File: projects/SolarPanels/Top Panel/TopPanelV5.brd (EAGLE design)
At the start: 99.5 x 99.5 mm, 41 parts

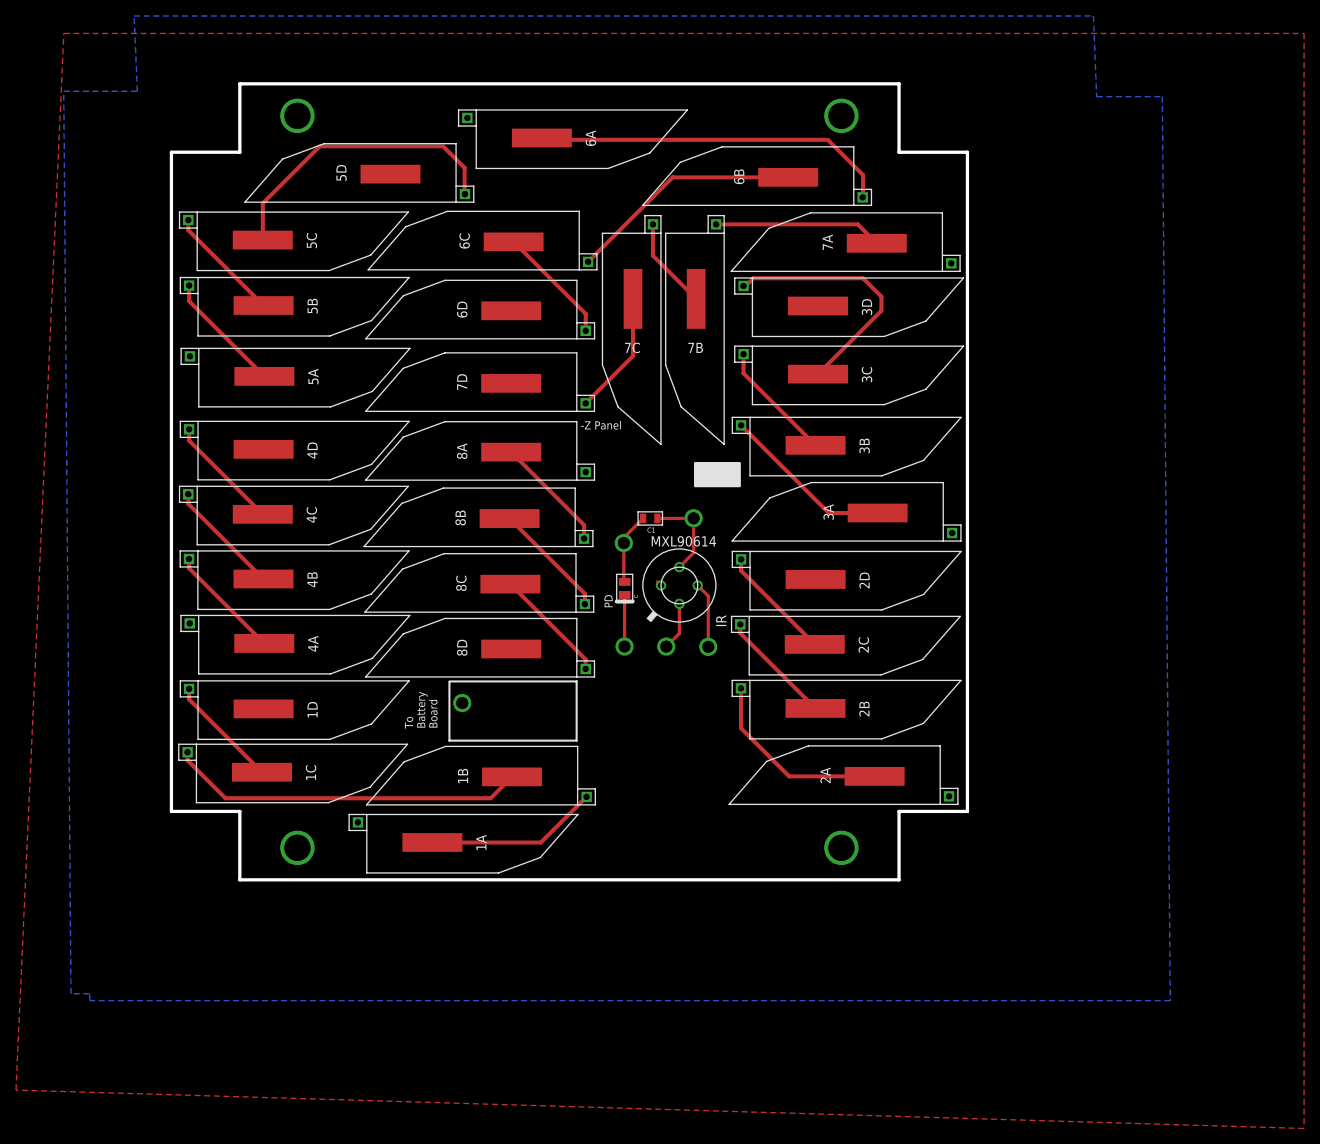
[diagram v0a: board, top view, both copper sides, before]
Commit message: Completed TopPanelV5 with new board dimensions and cells. Ready for rewview/fab
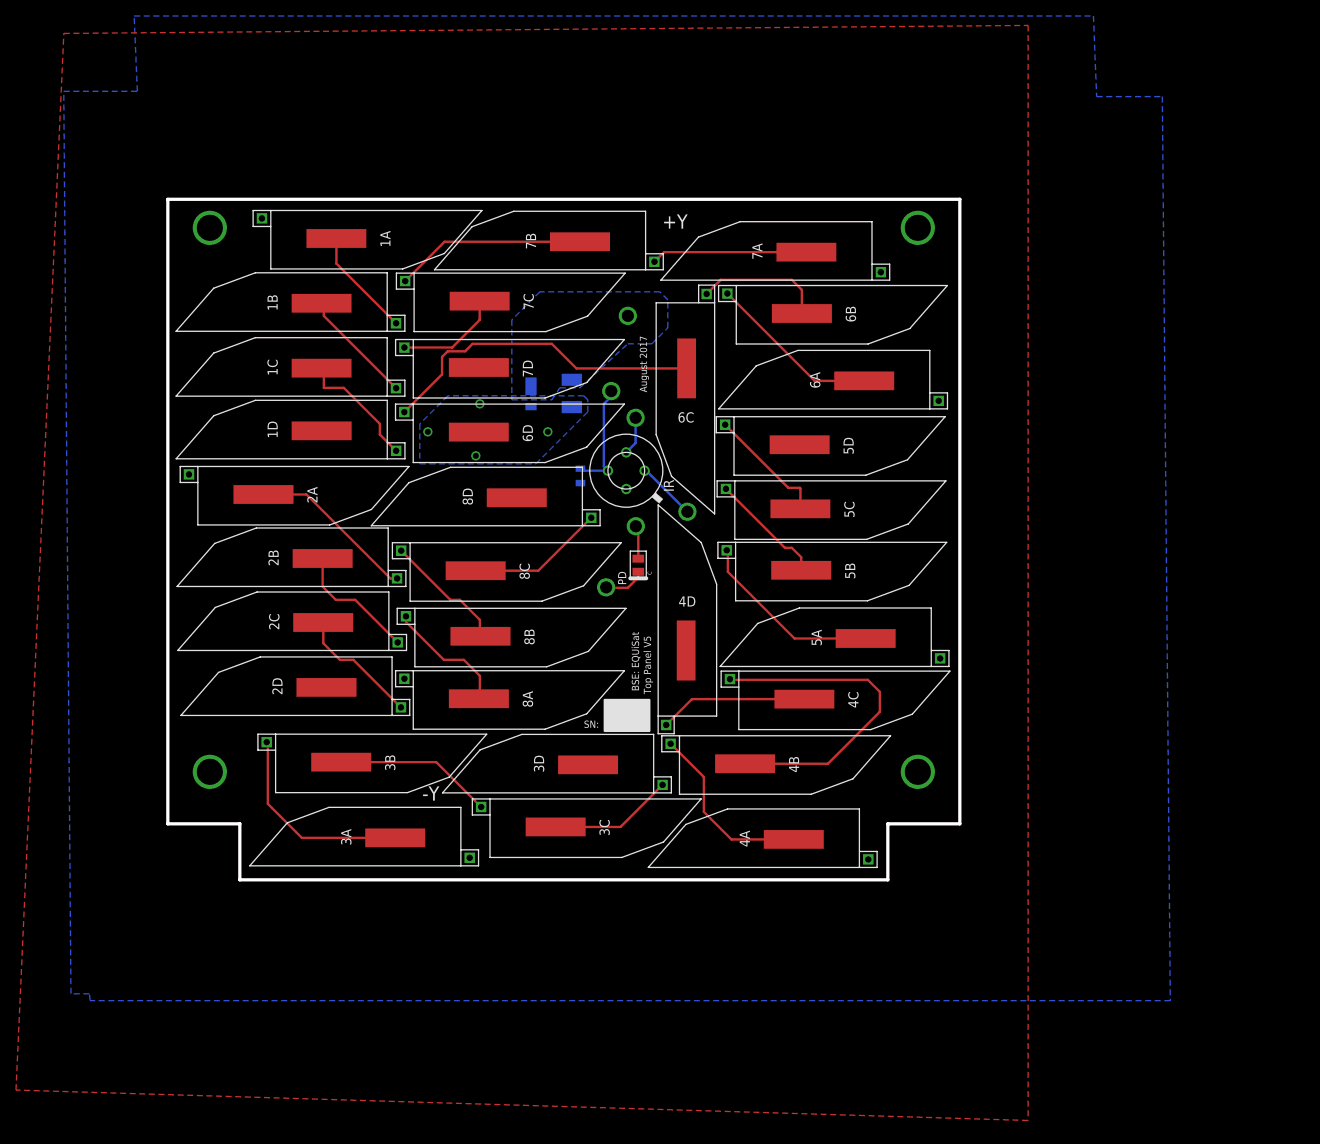
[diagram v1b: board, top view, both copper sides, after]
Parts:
- added D1: DFLS130L, BrownSpaceEngineering:PWRDI-123
- added R1: 0R, BrownSpaceEngineering:1210
- V1: value SP-PWR -> SP-PWR-OUT
- moved 2A 77.4 mm to (7.17, 49.1), turned to 180 degrees
- moved 1A 76.4 mm to (16.3, 81.1)
- moved 5A 75.2 mm to (74.0, 29.2), turned to 0 degrees
- moved 5C 75.1 mm to (74.3, 47.3)
- moved 5B 74.9 mm to (74.4, 39.6)
- moved 3A 72.7 mm to (15.2, 4.29)
- moved 2B 72.0 mm to (6.13, 39.2), turned to 0 degrees
- moved 4C 71.5 mm to (74.8, 23.6)
- moved 3B 71.3 mm to (16.9, 15.7)
- moved 2D 71.3 mm to (6.61, 23.1), turned to 0 degrees
- moved 3D 70.0 mm to (39.3, 13.4), turned to 0 degrees
- moved 2C 69.9 mm to (6.21, 31.2), turned to 0 degrees
- moved 5D 67.6 mm to (74.2, 55.4), turned to 180 degrees
- moved 3C 65.4 mm to (43.7, 7.57)
- moved 4B 64.5 mm to (67.4, 15.5)
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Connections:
- new net SP-PWR-OUT: D1.C, R1.P$2, V1.P$1
- net SP-PWR: now also D1.A, R1.P$1; no longer V1.P$1
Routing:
- net N$13: track 44.6 -> 15.0 mm
- net N$25: track 397.8 -> 368.1 mm
- net N$16: track 14.5 -> 41.4 mm
- net N$6: track 14.9 -> 41.4 mm
- net N$12: track 44.9 -> 21.6 mm
- net N$5: track 37.2 -> 15.3 mm
- net N$3: track 31.6 -> 15.5 mm
- net N$18: track 29.4 -> 16.6 mm
- net N$21: track 11.5 -> 23.9 mm
- net N$10: track 14.5 -> 22.9 mm
- net N$11: track 15.3 -> 23.4 mm
- net N$7: track 21.6 -> 13.7 mm
- net GND: track 9.61 -> 4.36 mm
- net N$15: track 15.1 -> 19.8 mm
- net N$1: track 14.2 -> 18.8 mm
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- added copper zone on layer 16, net SP-PWR
- added copper zone on layer 16, net SP-PWR-OUT
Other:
- board size 99.5 x 99.5 mm -> 99 x 85.1 mm
- board text added: "+Y"
- board text added: "-Y"
- board text added: "August 2017"
- board text added: "BSE: EQUiSat"
- board text added: "Brown Space Engineering: EQUiSat"
- board text added: "SN:"
- board text added: "Top Panel V5"
- board text removed: "-Z Panel"
- board text removed: "To Battery Board"

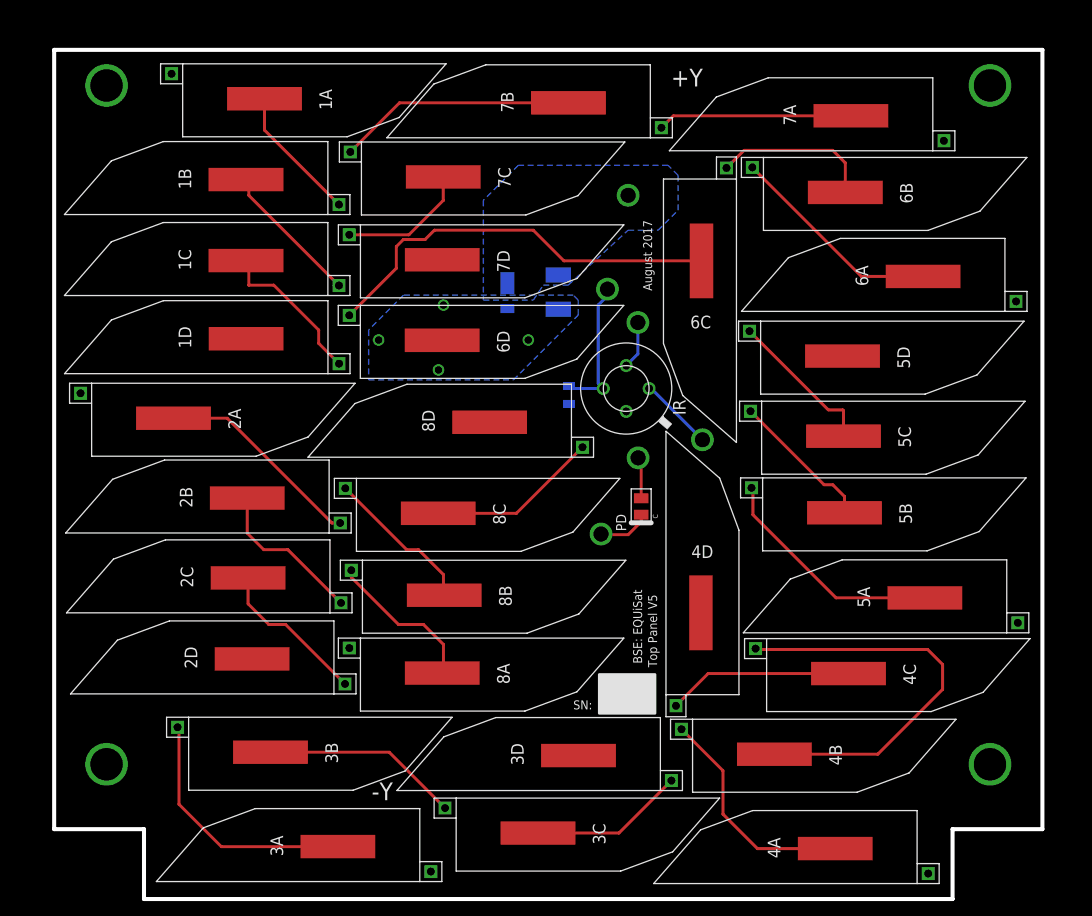
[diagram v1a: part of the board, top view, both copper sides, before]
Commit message: Modified Top Panel V5 layout to optimize for wiring.
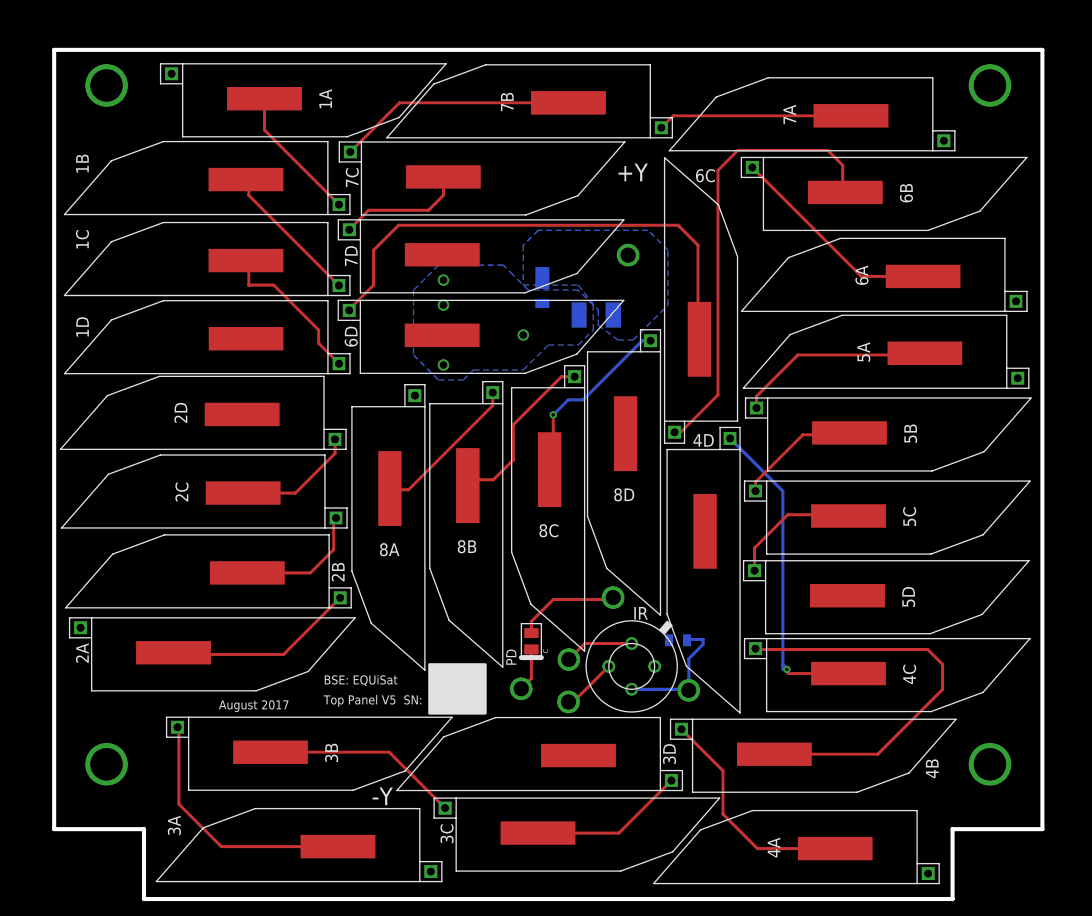
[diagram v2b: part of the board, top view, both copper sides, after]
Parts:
- moved V3 41.0 mm to (54.6, 20.9), turned to 180 degrees
- moved SDA 38.6 mm to (42.5, 19.7), turned to 90 degrees
- moved IR 27.8 mm to (48.9, 23.3), turned to 90 degrees
- moved C1 26.9 mm to (53.5, 25.9), turned to 180 degrees
- moved SCL 25.8 mm to (42.6, 24.0), turned to 90 degrees
- moved 2D 24.5 mm to (5.61, 47.6)
- moved 5A 24.5 mm to (74.0, 53.7)
- moved 5D 24.0 mm to (74.7, 31.4)
- moved 2A 23.5 mm to (7.17, 25.6)
- moved 8D 19.3 mm to (49.2, 42.4), turned to 90 degrees
- moved V6 17.4 mm to (37.8, 21.1)
- moved PD 17.4 mm to (39.2, 25.9)
- moved 8A 15.8 mm to (25.6, 36.9), turned to 90 degrees
- moved V4 14.2 mm to (47.0, 30.2)
- moved 2C 8.51 mm to (5.71, 39.7)
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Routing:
- net N$18: track 16.6 -> 45.4 mm
- net N$4: track 18.6 -> 32.1 mm, vias 0 -> 1
- net N$6: track 41.4 -> 52.1 mm
- net GND: track 4.36 -> 10.3 mm
- net N$11: track 23.4 -> 19.8 mm
- net N$2: track 15.6 -> 12.3 mm
- net N$14: track 15.8 -> 12.9 mm
- net N$17: track 14.6 -> 12.3 mm
- net N$5: track 15.3 -> 13.1 mm
- net N$8: track 21.1 -> 19.1 mm
- net N$24: track 15.5 -> 17.3 mm
- net N$22: track 17.2 -> 18.4 mm, vias 0 -> 1
- net 3V3-IR: track 14.1 -> 13.1 mm
- net PD-OUT: track 5.29 -> 4.37 mm
- net SDA: track 4.80 -> 5.51 mm
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
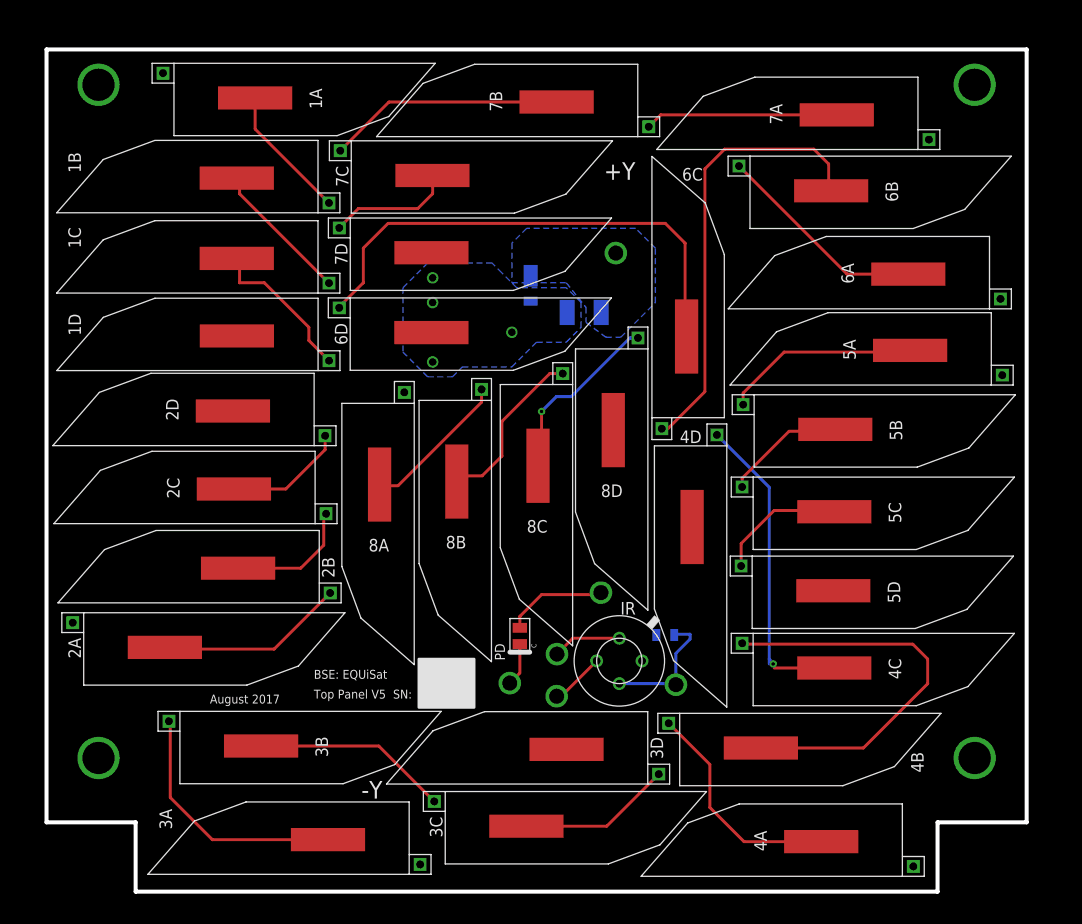
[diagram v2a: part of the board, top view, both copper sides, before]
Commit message: Edits to TopPanelV5 per Caelan's suggestions.
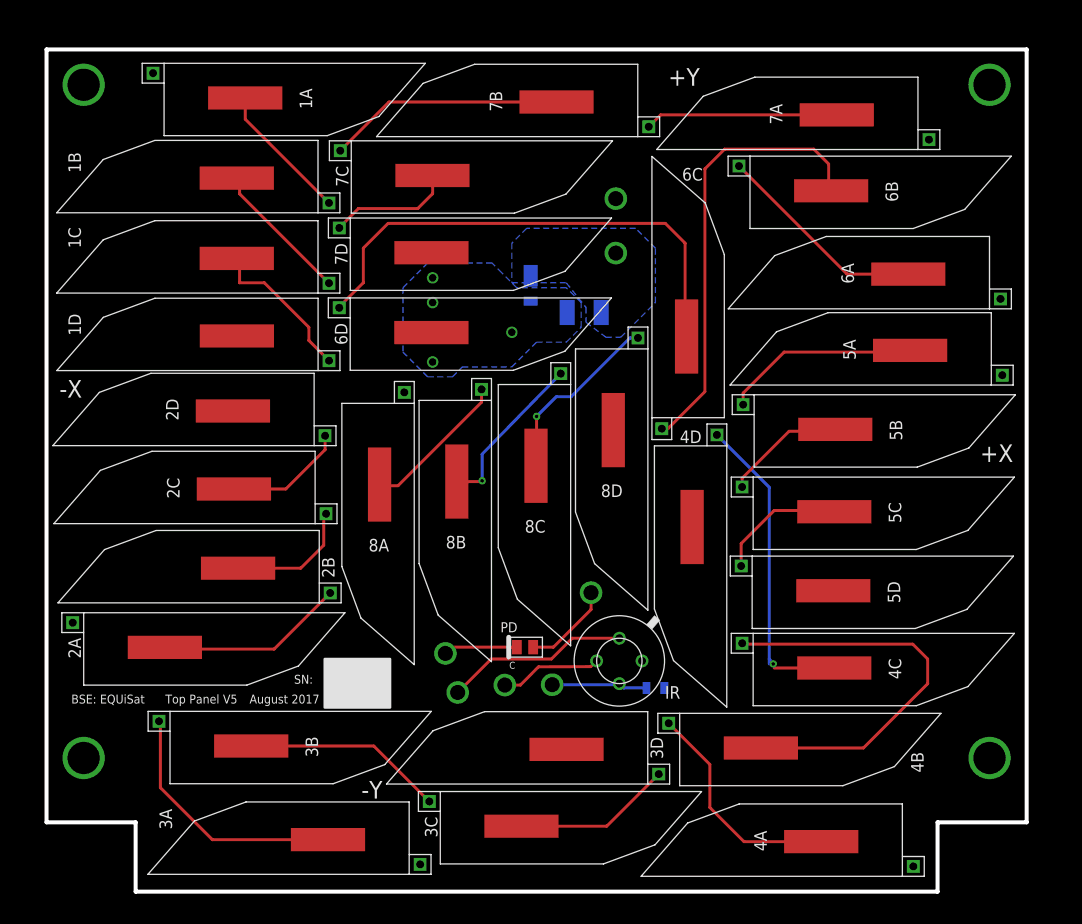
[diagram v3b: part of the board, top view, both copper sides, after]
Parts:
- added V2: GND, BrownSpaceEngineering:VIA-60MIL
- moved V3 12.5 mm to (42.1, 20.9)
- moved SCL 10.7 mm to (32.5, 20.1), turned to 180 degrees
- moved V6 7.16 mm to (31.3, 24.1)
- moved C1 5.44 mm to (52.5, 20.6), turned to 0 degrees
- moved SDA 5.36 mm to (37.3, 20.9), turned to 180 degrees
- moved PD 1.61 mm to (39.4, 24.3), turned to 0 degrees
- moved 1A 1.00 mm to (15.3, 81.1)
- moved 3B 1.00 mm to (15.9, 15.7)
- moved V4 1.00 mm to (46.0, 30.2)
- moved 3C 0.50 mm to (43.2, 7.57)
- moved 8C 0.20 mm to (41.4, 38.8)
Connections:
- net GND: now also V2.P$1
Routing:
- net SCL: track 6.97 -> 18.6 mm
- net SDA: track 5.51 -> 10.3 mm
- net 3V3-IR: track 13.1 -> 9.76 mm
- net PD-OUT: track 4.37 -> 7.48 mm
- net GND: track 10.3 -> 9.13 mm
- net N$24: track 17.3 -> 16.7 mm, vias 0 -> 1
- net N$3: track 15.5 -> 16.0 mm
- net N$15: track 19.8 -> 20.3 mm
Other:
- board text added: "+X"
- board text added: "-X"
